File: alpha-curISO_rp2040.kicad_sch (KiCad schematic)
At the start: 23 parts, among them J2 SWD, U1 RP2040, U5 74AHCT1G125

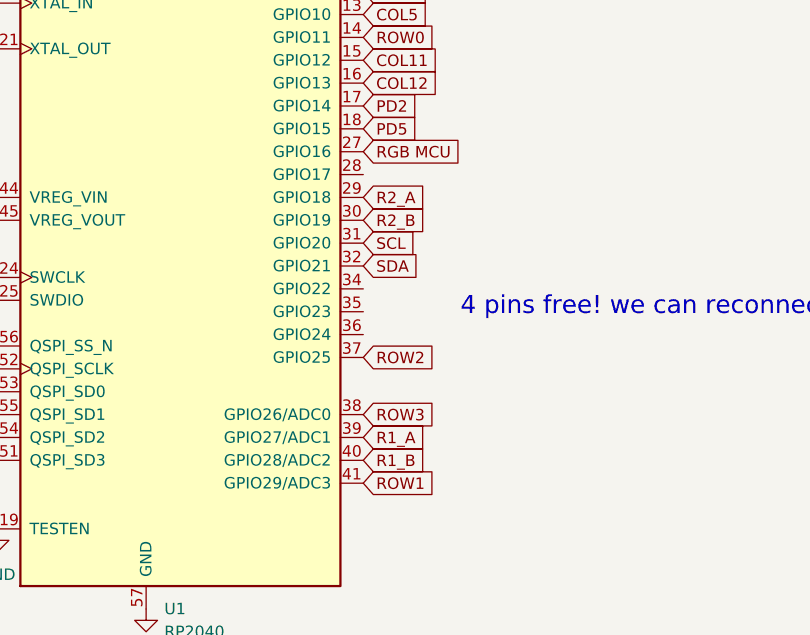
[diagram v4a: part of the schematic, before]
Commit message: rgb fixed, rotaries separately reconnected
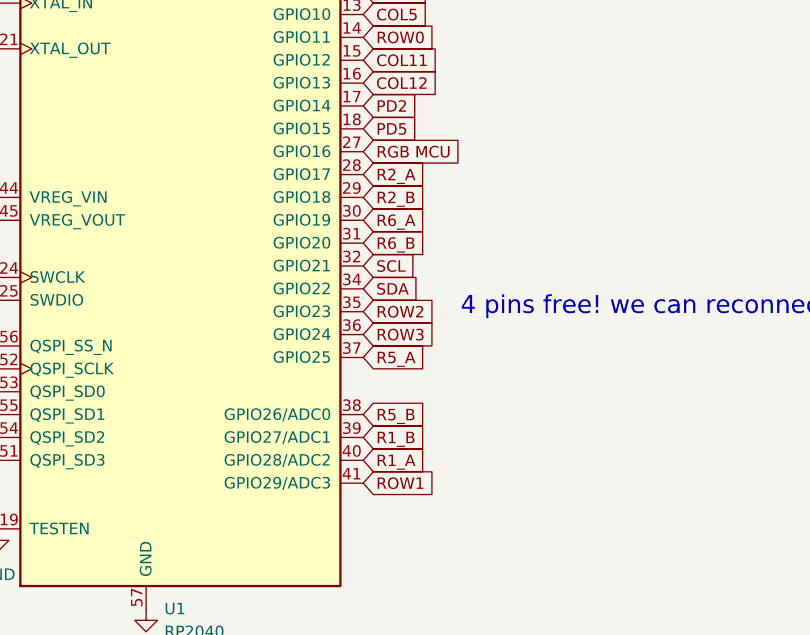
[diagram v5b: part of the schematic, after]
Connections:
- net R1_A: now also U1.40 (GPIO28/ADC2); no longer U1.39 (GPIO27/ADC1)
- net R1_B: now also U1.39 (GPIO27/ADC1); no longer U1.40 (GPIO28/ADC2)
- net R2_A: now also U1.28 (GPIO17); no longer U1.29 (GPIO18)
- net R2_B: now also U1.29 (GPIO18); no longer U1.30 (GPIO19)
- net ROW2: now also U1.35 (GPIO23); no longer U1.37 (GPIO25)
- net ROW3: now also U1.36 (GPIO24); no longer U1.38 (GPIO26/ADC0)
- net SCL: now also U1.32 (GPIO21); no longer U1.31 (GPIO20)
- net SDA: now also U1.34 (GPIO22); no longer U1.32 (GPIO21)
- new net R5_A: U1.37 (GPIO25)
- new net R5_B: U1.38 (GPIO26/ADC0)
- new net R6_A: U1.30 (GPIO19)
- new net R6_B: U1.31 (GPIO20)
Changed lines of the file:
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@@
     (effects (font (size 1.27 1.27)) (justify left bottom))
   )
-  (global_label "SCL" (shape input) (at 80.01 87.63 0) (fields_autoplaced)
-    (effects (font (size 1.27 1.27)) (justify left))
-    (property "Intersheet References" "${INTERSHEET_REFS}" (id 0) (at 85.9307 87.7094 0)
+  (global_label "SCL" (shape input) (at 80.01 90.17 0) (fields_autoplaced)
+    (effects (font (size 1.27 1.27)) (justify left))
+    (property "Intersheet References" "${INTERSHEET_REFS}" (id 0) (at 85.9307 90.2494 0)
       (effects (font (size 1.27 1.27)) (justify left) hide)
     )
@@
     )
   )
-  (global_label "R2_B" (shape input) (at 80.01 85.09 0) (fields_autoplaced)
-    (effects (font (size 1.27 1.27)) (justify left))
-    (property "Intersheet References" "${INTERSHEET_REFS}" (id 0) (at 87.1402 85.1694 0)
+  (global_label "R2_B" (shape input) (at 80.01 82.55 0) (fields_autoplaced)
+    (effects (font (size 1.27 1.27)) (justify left))
+    (property "Intersheet References" "${INTERSHEET_REFS}" (id 0) (at 87.1402 82.6294 0)
       (effects (font (size 1.27 1.27)) (justify left) hide)
     )
@@
     )
   )
+  (global_label "R6_A" (shape input) (at 80.01 85.09 0) (fields_autoplaced)
+    (effects (font (size 1.27 1.27)) (justify left))
+    (property "Intersheet References" "${INTERSHEET_REFS}" (id 0) (at 86.9588 85.1694 0)
+      (effects (font (size 1.27 1.27)) (justify left) hide)
+    )
+  )
   (global_label "ROW1" (shape input) (at 80.01 114.3 0) (fields_autoplaced)
     (effects (font (size 1.27 1.27)) (justify left))
@@
     )
   )
-  (global_label "ROW2" (shape input) (at 80.01 100.33 0) (fields_autoplaced)
-    (effects (font (size 1.27 1.27)) (justify left))
-    (property "Intersheet References" "${INTERSHEET_REFS}" (id 0) (at 87.6845 100.4094 0)
+  (global_label "ROW2" (shape input) (at 80.01 95.25 0) (fields_autoplaced)
+    (effects (font (size 1.27 1.27)) (justify left))
+    (property "Intersheet References" "${INTERSHEET_REFS}" (id 0) (at 87.6845 95.3294 0)
       (effects (font (size 1.27 1.27)) (justify left) hide)
     )
@@
     )
   )
-  (global_label "R2_A" (shape input) (at 80.01 82.55 0) (fields_autoplaced)
-    (effects (font (size 1.27 1.27)) (justify left))
-    (property "Intersheet References" "${INTERSHEET_REFS}" (id 0) (at 86.9588 82.6294 0)
+  (global_label "R2_A" (shape input) (at 80.01 80.01 0) (fields_autoplaced)
+    (effects (font (size 1.27 1.27)) (justify left))
+    (property "Intersheet References" "${INTERSHEET_REFS}" (id 0) (at 86.9588 80.0894 0)
       (effects (font (size 1.27 1.27)) (justify left) hide)
     )
@@
     )
   )
+  (global_label "R5_A" (shape input) (at 80.01 100.33 0) (fields_autoplaced)
+    (effects (font (size 1.27 1.27)) (justify left))
+    (property "Intersheet References" "${INTERSHEET_REFS}" (id 0) (at 86.9588 100.4094 0)
+      (effects (font (size 1.27 1.27)) (justify left) hide)
+    )
+  )
   (global_label "SD3" (shape input) (at 39.37 111.76 180) (fields_autoplaced)
     (effects (font (size 1.27 1.27)) (justify right))
@@
     )
   )
-  (global_label "SDA" (shape input) (at 80.01 90.17 0) (fields_autoplaced)
-    (effects (font (size 1.27 1.27)) (justify left))
-    (property "Intersheet References" "${INTERSHEET_REFS}" (id 0) (at 85.9912 90.2494 0)
+  (global_label "SDA" (shape input) (at 80.01 92.71 0) (fields_autoplaced)
+    (effects (font (size 1.27 1.27)) (justify left))
+    (property "Intersheet References" "${INTERSHEET_REFS}" (id 0) (at 85.9912 92.7894 0)
       (effects (font (size 1.27 1.27)) (justify left) hide)
     )
@@
     )
   )
-  (global_label "ROW3" (shape input) (at 80.01 106.68 0) (fields_autoplaced)
-    (effects (font (size 1.27 1.27)) (justify left))
-    (property "Intersheet References" "${INTERSHEET_REFS}" (id 0) (at 87.6845 106.7594 0)
+  (global_label "ROW3" (shape input) (at 80.01 97.79 0) (fields_autoplaced)
+    (effects (font (size 1.27 1.27)) (justify left))
+    (property "Intersheet References" "${INTERSHEET_REFS}" (id 0) (at 87.6845 97.8694 0)
       (effects (font (size 1.27 1.27)) (justify left) hide)
     )
@@
     )
   )
+  (global_label "R6_B" (shape input) (at 80.01 87.63 0) (fields_autoplaced)
+    (effects (font (size 1.27 1.27)) (justify left))
+    (property "Intersheet References" "${INTERSHEET_REFS}" (id 0) (at 87.1402 87.7094 0)
+      (effects (font (size 1.27 1.27)) (justify left) hide)
+    )
+  )
   (global_label "XTAL_OUT" (shape input) (at 39.37 66.04 180) (fields_autoplaced)
     (effects (font (size 1.27 1.27)) (justify right))
@@
     )
   )
+  (global_label "R5_B" (shape input) (at 80.01 106.68 0) (fields_autoplaced)
+    (effects (font (size 1.27 1.27)) (justify left))
+    (property "Intersheet References" "${INTERSHEET_REFS}" (id 0) (at 87.1402 106.7594 0)
+      (effects (font (size 1.27 1.27)) (justify left) hide)
+    )
+  )
   (global_label "PD5" (shape input) (at 80.01 74.93 0) (fields_autoplaced)
     (effects (font (size 1.27 1.27)) (justify left))
@@
     )
   )
-  (global_label "R1_A" (shape input) (at 80.01 109.22 0) (fields_autoplaced)
-    (effects (font (size 1.27 1.27)) (justify left))
-    (property "Intersheet References" "${INTERSHEET_REFS}" (id 0) (at 86.9588 109.2994 0)
+  (global_label "R1_A" (shape input) (at 80.01 111.76 0) (fields_autoplaced)
+    (effects (font (size 1.27 1.27)) (justify left))
+    (property "Intersheet References" "${INTERSHEET_REFS}" (id 0) (at 86.9588 111.8394 0)
       (effects (font (size 1.27 1.27)) (justify left) hide)
     )
@@
     )
   )
-  (global_label "R1_B" (shape input) (at 80.01 111.76 0) (fields_autoplaced)
-    (effects (font (size 1.27 1.27)) (justify left))
-    (property "Intersheet References" "${INTERSHEET_REFS}" (id 0) (at 87.1402 111.8394 0)
+  (global_label "R1_B" (shape input) (at 80.01 109.22 0) (fields_autoplaced)
+    (effects (font (size 1.27 1.27)) (justify left))
+    (property "Intersheet References" "${INTERSHEET_REFS}" (id 0) (at 87.1402 109.2994 0)
       (effects (font (size 1.27 1.27)) (justify left) hide)
     )
@@
   (symbol (lib_id "power:GND") (at 266.065 184.785 90) (unit 1)
     (in_bom yes) (on_board yes) (fields_autoplaced)
-    (property "Reference" "#PWR?" (id 0) (at 272.415 184.785 0)
+    (property "Reference" "#PWR0146" (id 0) (at 272.415 184.785 0)
       (effects (font (size 1.27 1.27)) hide)
     )
@@
       (reference "#PWR0145") (unit 1) (value "+5V") (footprint "")
     )
+    (path "/154d94df-cae8-4677-ab8f-64c7641a0ed8"
+      (reference "#PWR0146") (unit 1) (value "GND") (footprint "")
+    )
     (path "/ed815977-8ce9-43bf-9f7d-c601496617ea/a29ce2bd-7f3e-4f4b-b2fc-e02b47b0b88b"
       (reference "#PWR0147") (unit 1) (value "GND") (footprint "")
     )
-    (path "/154d94df-cae8-4677-ab8f-64c7641a0ed8"
-      (reference "#PWR?") (unit 1) (value "GND") (footprint "")
-    )
     (path "/ed815977-8ce9-43bf-9f7d-c601496617ea/cce79384-81e6-4921-84d5-1511ce8fbc31"
